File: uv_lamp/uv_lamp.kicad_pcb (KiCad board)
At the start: 2 copper layers, 165.1 x 121.9 mm, 178 parts, among them J1 Conn_01x03

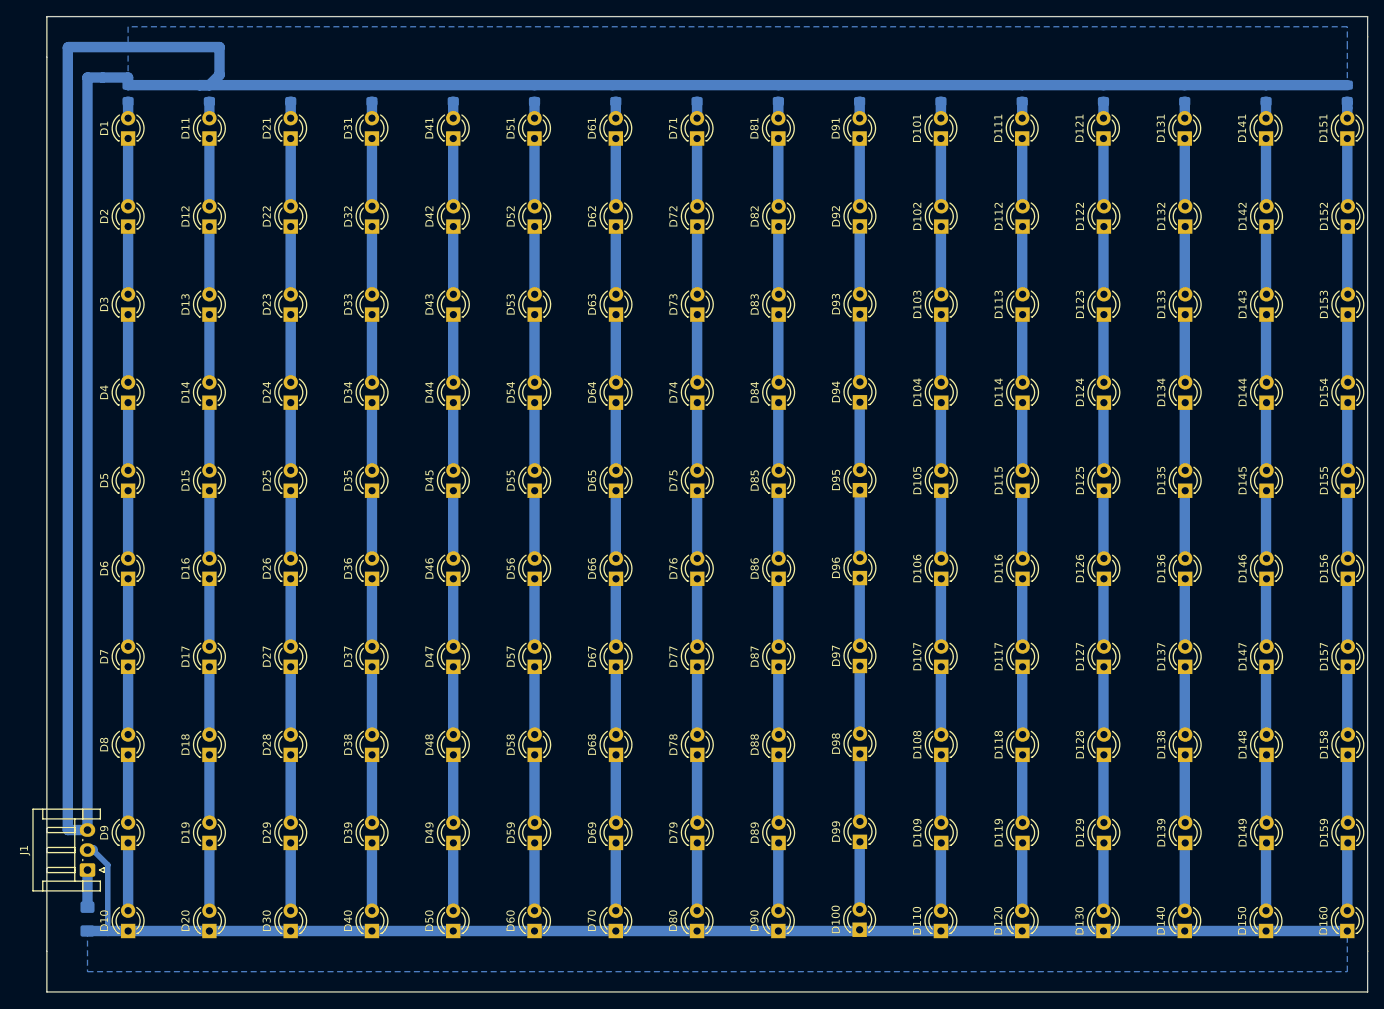
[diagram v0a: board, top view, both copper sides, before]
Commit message: 10mm led distance
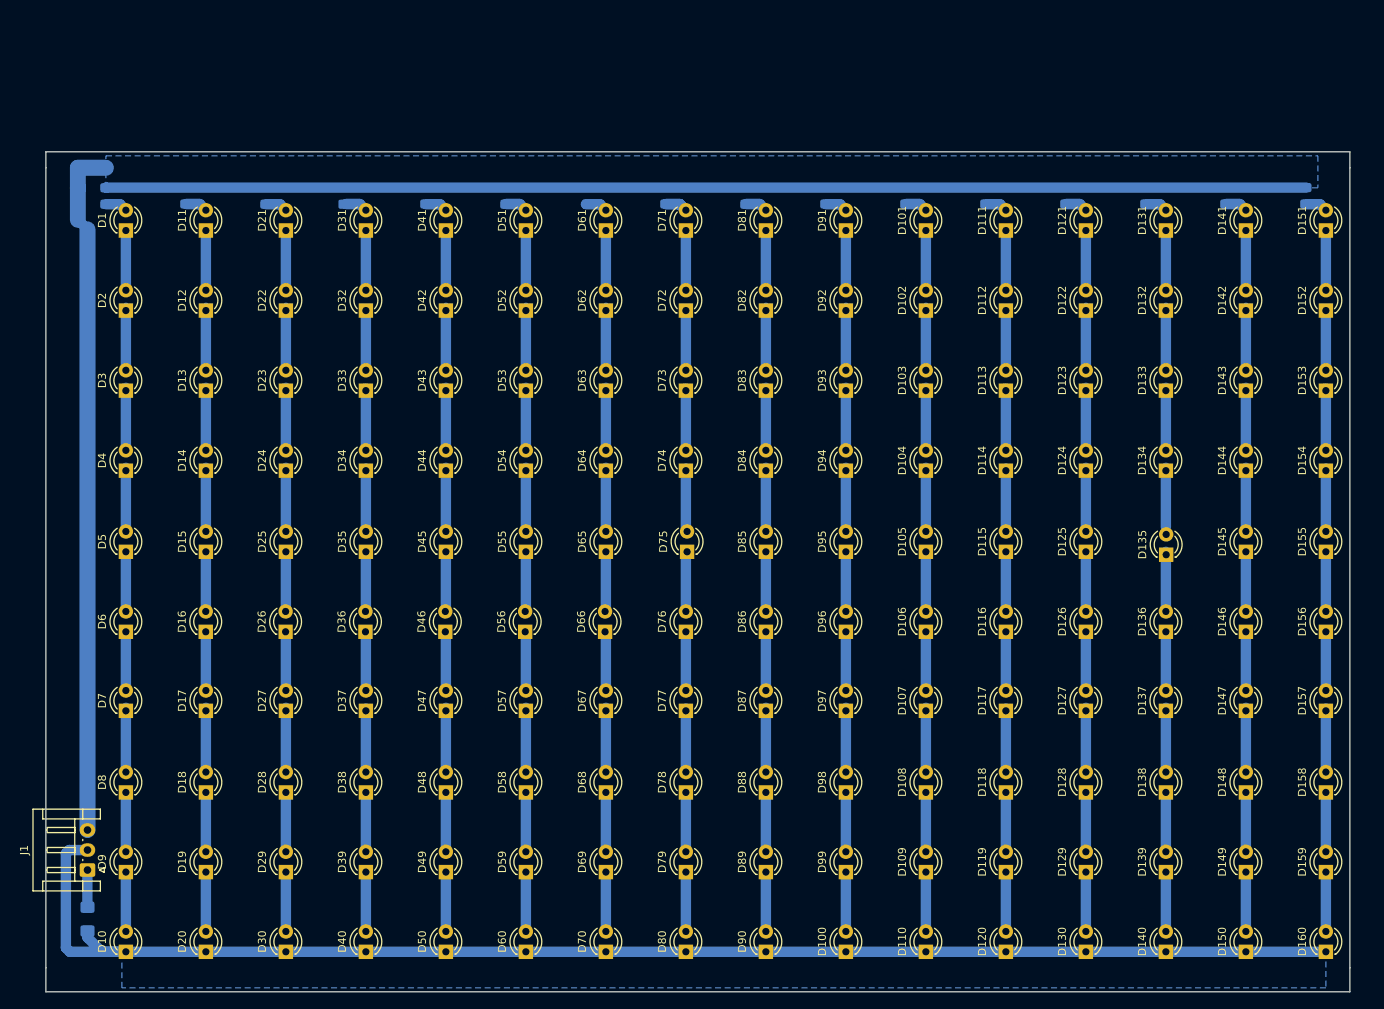
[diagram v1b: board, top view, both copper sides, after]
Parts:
- moved R16 13.8 mm to (228.5, 60.5)
- moved R15 13.8 mm to (218.5, 60.5)
- moved R14 13.7 mm to (208.5, 60.5)
- moved R13 13.6 mm to (198.5, 60.5)
- moved R12 13.6 mm to (188.5, 60.5)
- moved R11 13.5 mm to (178.5, 60.5)
- moved R10 13.5 mm to (168.5, 60.5)
- moved R9 13.5 mm to (158.5, 60.5)
- moved R8 13.4 mm to (148.5, 60.5)
- moved R6 13.3 mm to (128.5, 60.5)
- moved R4 13.3 mm to (108.3, 60.5)
- moved R7 13.3 mm to (138.7, 60.5)
- moved R5 13.3 mm to (118.5, 60.5)
- moved R3 13.2 mm to (98.5, 60.5)
- moved R2 13.1 mm to (88.5, 60.5)
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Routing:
- net Net-(J1-Pad3): track 378.3 -> 236.8 mm
- net Net-(D10-Pad1): track 169.0 -> 178.7 mm
- net Net-(D71-Pad2): track 2.08 -> 5.63 mm
- net Net-(D21-Pad1): track 8.47 -> 7.42 mm
- net Net-(D11-Pad1): track 8.47 -> 7.42 mm
- net Net-(D79-Pad1): track 8.47 -> 7.42 mm
- net Net-(D39-Pad1): track 8.47 -> 7.42 mm
- net Net-(D159-Pad1): track 8.47 -> 7.42 mm
- net Net-(D119-Pad1): track 8.47 -> 7.42 mm
- net Net-(D89-Pad1): track 8.47 -> 7.42 mm
- net Net-(D69-Pad1): track 8.47 -> 7.42 mm
- net Net-(D59-Pad1): track 8.47 -> 7.42 mm
- net Net-(D49-Pad1): track 8.47 -> 7.42 mm
- net Net-(D29-Pad1): track 8.47 -> 7.42 mm
- net Net-(D19-Pad1): track 8.47 -> 7.42 mm
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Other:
- board size 165.1 x 121.9 mm -> 163 x 105 mm
